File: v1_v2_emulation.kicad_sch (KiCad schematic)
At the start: 7 parts, among them CN5 LED, IC20 7407, IC65 D65101GD110

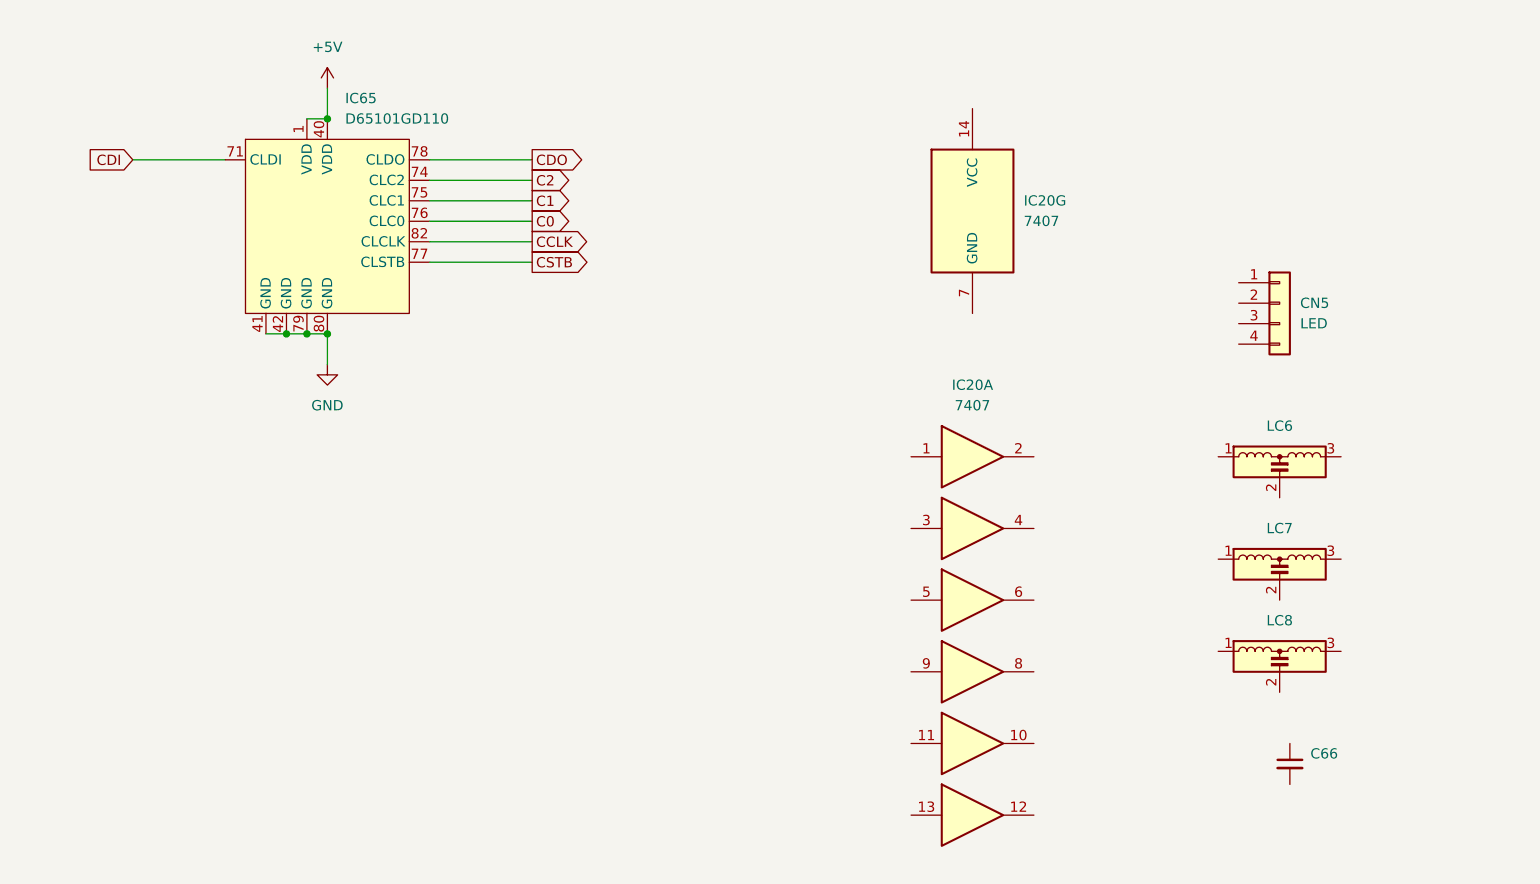
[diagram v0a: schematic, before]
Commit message: add CN2 FDD connector
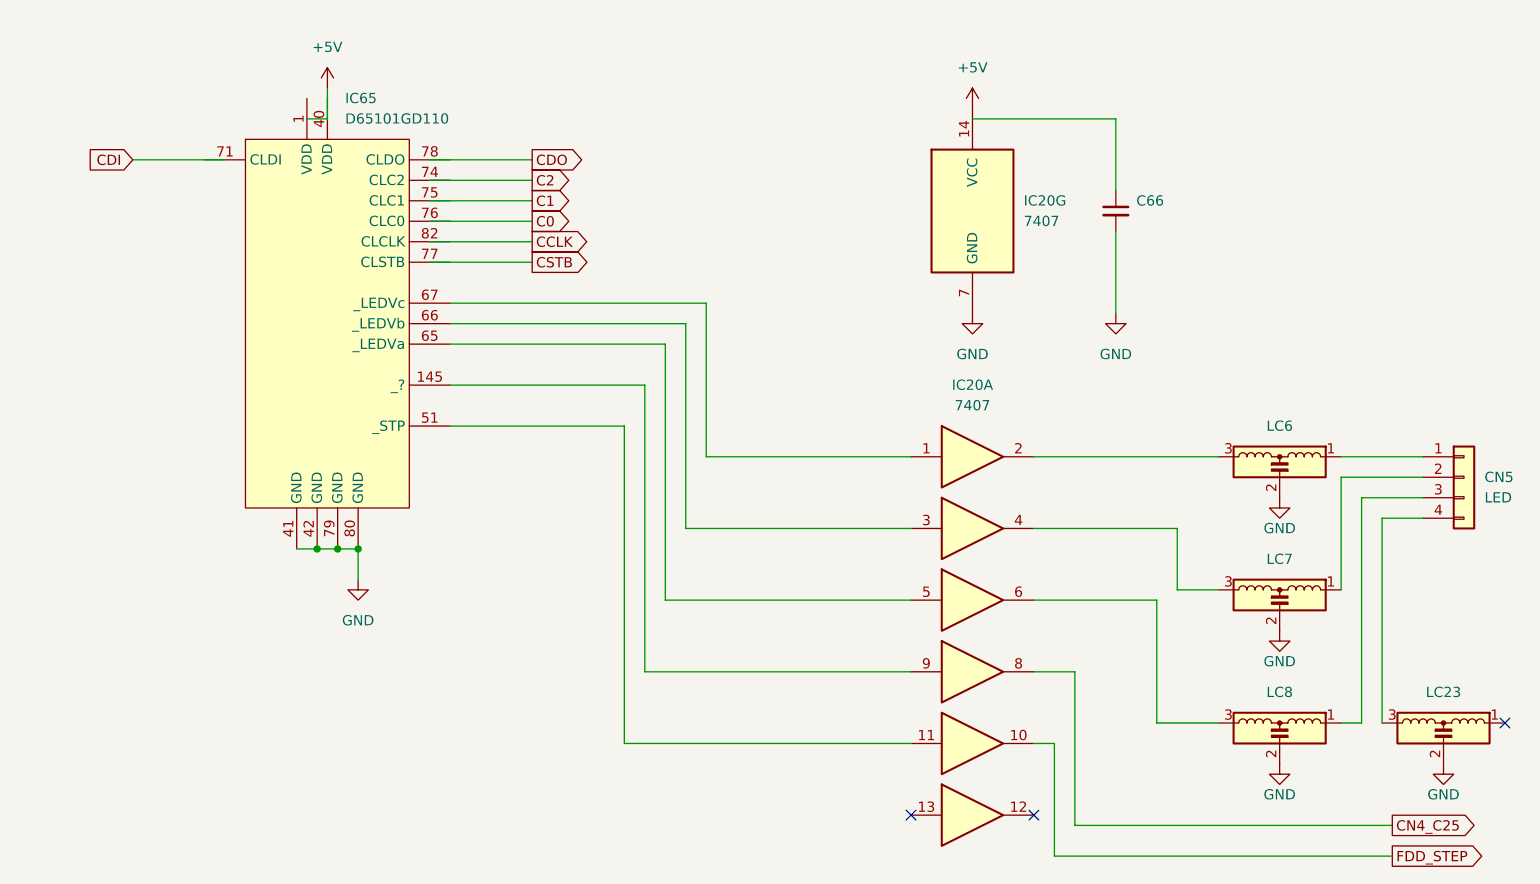
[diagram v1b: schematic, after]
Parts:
- added LC23: Filter_EMI_LCL, 88va_Library:Filter, symbol Device:Filter_EMI_LCL
- C66: footprint (none) -> Capacitor_SMD:C_1206_3216Metric
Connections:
- net +5V: now also IC20.14 (VCC); no longer IC65.1 (VDD), IC65.40 (VDD)
- net C0: no longer IC65.76 (CLC0)
- net C1: no longer IC65.75 (CLC1)
- net C2: no longer IC65.74 (CLC2)
- net CCLK: no longer IC65.82 (CLCLK)
- net CDI: no longer IC65.71 (CLDI)
- net CDO: no longer IC65.78 (CLDO)
- net CSTB: no longer IC65.77 (CLSTB)
- net GND: now also C66.2, IC20.7 (GND), LC6.2, LC7.2, LC8.2, LC23.2
- net FDD_STEP: now reaches IC20.10
- net at IC20.11: now also IC65.51 (_STP)
- net CN4_C25: now reaches IC20.8
- net at IC20.9: now also IC65.145 (_?)
- net at IC20.5: now also IC65.65 (_LEDVa)
- net at IC20.6: now also LC8.3
- net at IC20.3: now also IC65.66 (_LEDVb)
- net at IC20.4: now also LC7.3
- net at LC7.1: now also CN5.2 (Pin_2)
- net at LC6.1: now also CN5.1 (Pin_1)
- net at LC6.3: now also IC20.2
- net at IC20.1: now also IC65.67 (_LEDVc)
- net at LC8.1: now also CN5.3 (Pin_3)
- net at CN5.4 (Pin_4): now also LC23.3
- no-connect marks 0 -> 3
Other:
- moved on the sheet: C66, CN5, LC7, LC8

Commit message: add CN4 TEXT BUS
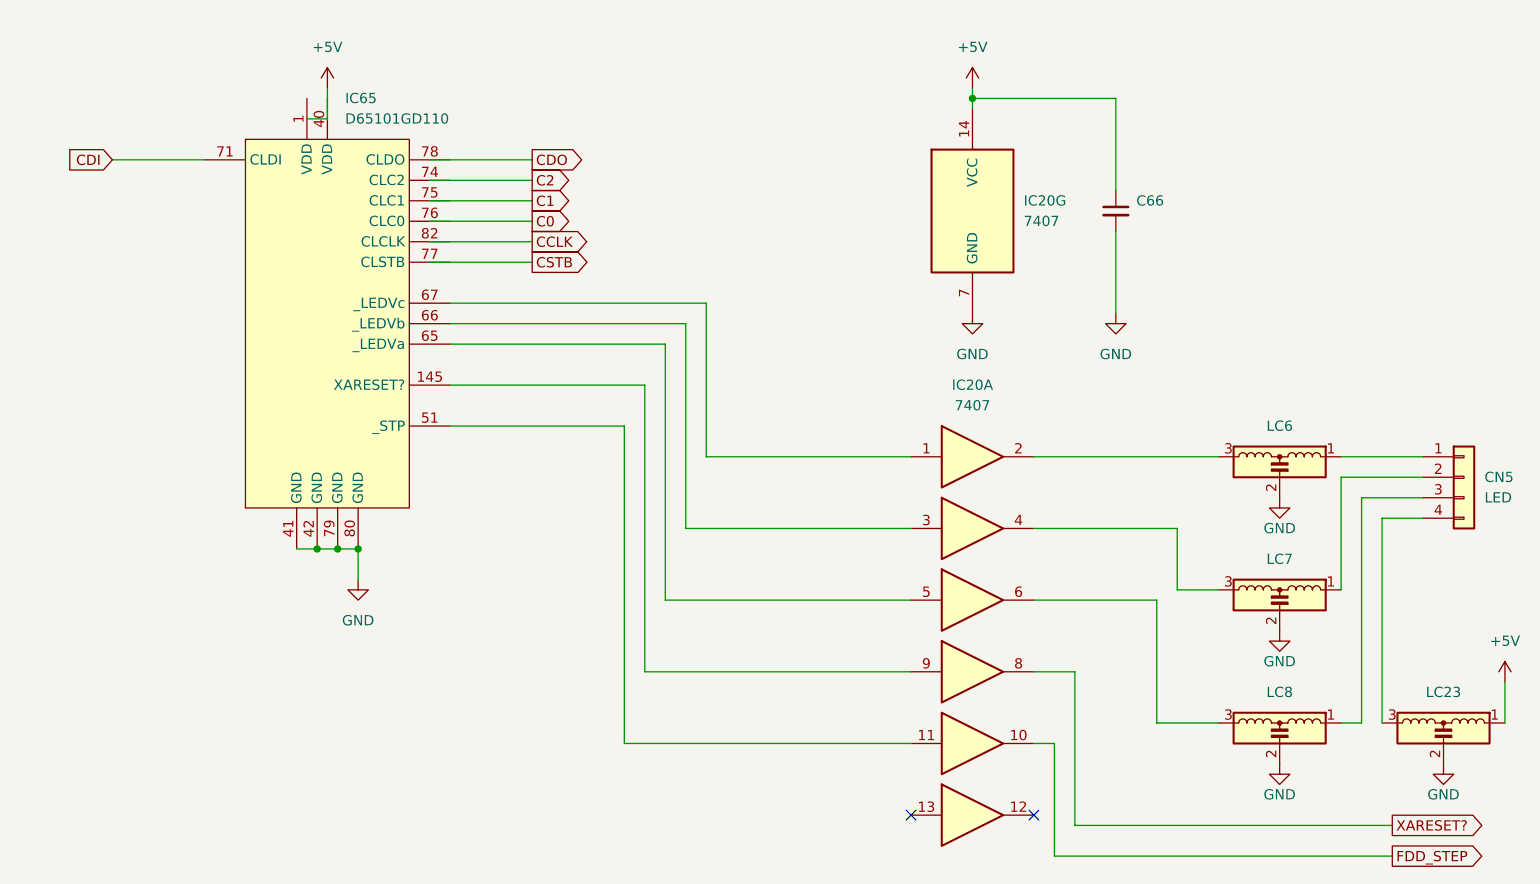
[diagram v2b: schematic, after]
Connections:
- net +5V: now also C66.1, LC23.1
- net CDI: now also IC65.71 (CLDI)
- net CN4_C25 renamed XARESET?
- no-connect marks 3 -> 2
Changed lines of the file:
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@@
   (junction (at 135.89 125.73) (diameter 0) (color 0 0 0 0)
+  )
+  (junction (at 217.17 69.85) (diameter 0) (color 0 0 0 0)
   )
   (junction (at 140.97 125.73) (diameter 0) (color 0 0 0 0)
@@
   (no_connect (at 224.79 158.75))
   (no_connect (at 209.55 158.75))
-  (no_connect (at 283.21 147.32))
-  (wire (pts (xy 234.95 72.39) (xy 234.95 81.28))
+  (wire (pts (xy 234.95 69.85) (xy 234.95 81.28))
     (stroke (width 0) (type default))
   )
@@
     (stroke (width 0) (type default))
   )
-  (wire (pts (xy 217.17 72.39) (xy 234.95 72.39))
+  (wire (pts (xy 217.17 69.85) (xy 234.95 69.85))
+    (stroke (width 0) (type default))
+  )
+  (wire (pts (xy 217.17 69.85) (xy 217.17 71.12))
     (stroke (width 0) (type default))
   )
@@
     (stroke (width 0) (type default))
   )
+  (wire (pts (xy 217.17 68.58) (xy 217.17 69.85))
+    (stroke (width 0) (type default))
+  )
   (wire (pts (xy 224.79 132.08) (xy 240.03 132.08))
     (stroke (width 0) (type default))
@@
     (stroke (width 0) (type default))
   )
-  (wire (pts (xy 113.03 77.47) (xy 124.46 77.47))
+  (wire (pts (xy 110.49 77.47) (xy 121.92 77.47))
     (stroke (width 0) (type default))
   )
@@
     (stroke (width 0) (type default))
   )
+  (wire (pts (xy 283.21 142.24) (xy 283.21 147.32))
+    (stroke (width 0) (type default))
+  )
   (wire (pts (xy 179.07 132.08) (xy 209.55 132.08))
     (stroke (width 0) (type default))
@@
     (stroke (width 0) (type default))
   )
-  (global_label "CN4_C25" (shape output) (at 269.24 160.02 0) (fields_autoplaced)
+  (global_label "XARESET?" (shape output) (at 269.24 160.02 0) (fields_autoplaced)
     (effects (font (size 1.27 1.27)) (justify left))
-    (property "Intersheetrefs" "${INTERSHEET_REFS}" (at 280.6918 160.02 0)
+    (property "Intersheetrefs" "${INTERSHEET_REFS}" (at 281.357 160.02 0)
       (effects (font (size 1.27 1.27)) (justify left) hide)
     )
@@
     )
   )
-  (global_label "CDI" (shape input) (at 113.03 77.47 180) (fields_autoplaced)
+  (global_label "CDI" (shape input) (at 110.49 77.47 180) (fields_autoplaced)
     (effects (font (size 1.27 1.27)) (justify right))
-    (property "Intersheetrefs" "${INTERSHEET_REFS}" (at 106.9 77.47 0)
+    (property "Intersheetrefs" "${INTERSHEET_REFS}" (at 104.36 77.47 0)
       (effects (font (size 1.27 1.27)) (justify right) hide)
     )
@@
     )
   )
+  (symbol (lib_id "power:+5V") (at 283.21 142.24 0) (unit 1)
+    (in_bom yes) (on_board yes) (dnp no) (fields_autoplaced)
+    (property "Reference" "#PWR024" (at 283.21 146.05 0)
+      (effects (font (size 1.27 1.27)) hide)
+    )
+    (property "Value" "+5V" (at 283.21 137.16 0)
+      (effects (font (size 1.27 1.27)))
+    )
+    (property "Footprint" "" (at 283.21 142.24 0)
+      (effects (font (size 1.27 1.27)) hide)
+    )
+    (property "Datasheet" "" (at 283.21 142.24 0)
+      (effects (font (size 1.27 1.27)) hide)
+    )
+    (pin "1")
+    (instances
+      (project "PWD665"
+        (path "/8cd193ae-a369-4130-9ba4-f2075fa60e2b/4936267e-2afc-4e41-be53-b97a571a33d1"
+          (reference "#PWR024") (unit 1)
+        )
+      )
+    )
+  )
   (symbol (lib_id "power:GND") (at 275.59 152.4 0) (unit 1)
     (in_bom yes) (on_board yes) (dnp no)
@@
     )
   )
-  (symbol (lib_id "power:+5V") (at 217.17 71.12 0) (unit 1)
-    (in_bom yes) (on_board yes) (dnp no) (fields_autoplaced)
-    (property "Reference" "#PWR018" (at 217.17 74.93 0)
-      (effects (font (size 1.27 1.27)) hide)
-    )
-    (property "Value" "+5V" (at 217.17 66.04 0)
-      (effects (font (size 1.27 1.27)))
-    )
-    (property "Footprint" "" (at 217.17 71.12 0)
-      (effects (font (size 1.27 1.27)) hide)
-    )
-    (property "Datasheet" "" (at 217.17 71.12 0)
-      (effects (font (size 1.27 1.27)) hide)
-    )
+  (symbol (lib_id "power:+5V") (at 217.17 68.58 0) (unit 1)
+    (in_bom yes) (on_board yes) (dnp no) (fields_autoplaced)
+    (property "Reference" "#PWR018" (at 217.17 72.39 0)
+      (effects (font (size 1.27 1.27)) hide)
+    )
+    (property "Value" "+5V" (at 217.17 63.5 0)
+      (effects (font (size 1.27 1.27)))
+    )
+    (property "Footprint" "" (at 217.17 68.58 0)
+      (effects (font (size 1.27 1.27)) hide)
+    )
+    (property "Datasheet" "" (at 217.17 68.58 0)
+      (effects (font (size 1.27 1.27)) hide)
+    )

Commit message: fix IC65
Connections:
- net +5V: now also IC65.1 (VDD), IC65.40 (VDD)
- net C0: now also IC65.76 (CLC0)
- net C1: now also IC65.75 (CLC1)
- net C2: now also IC65.74 (CLC2)
- net CCLK: now also IC65.82 (CLCLK)
- net CDO: now also IC65.78 (CLDO)
- net CSTB: now also IC65.77 (CLSTB)
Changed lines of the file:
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@@
   (junction (at 217.17 69.85) (diameter 0) (color 0 0 0 0)
+  )
+  (junction (at 137.16 69.85) (diameter 0) (color 0 0 0 0)
   )
   (junction (at 140.97 125.73) (diameter 0) (color 0 0 0 0)
@@
     (stroke (width 0) (type default))
   )
-  (wire (pts (xy 149.86 77.47) (xy 162.56 77.47))
+  (wire (pts (xy 152.4 77.47) (xy 162.56 77.47))
     (stroke (width 0) (type default))
   )
@@
     (stroke (width 0) (type default))
   )
-  (wire (pts (xy 137.16 68.58) (xy 137.16 72.39))
-    (stroke (width 0) (type default))
-  )
   (wire (pts (xy 217.17 69.85) (xy 234.95 69.85))
     (stroke (width 0) (type default))
@@
     (stroke (width 0) (type default))
   )
-  (wire (pts (xy 149.86 87.63) (xy 162.56 87.63))
+  (wire (pts (xy 152.4 87.63) (xy 162.56 87.63))
     (stroke (width 0) (type default))
   )
@@
     (stroke (width 0) (type default))
   )
-  (wire (pts (xy 134.62 72.39) (xy 137.16 72.39))
+  (wire (pts (xy 134.62 69.85) (xy 137.16 69.85))
     (stroke (width 0) (type default))
   )
@@
     (stroke (width 0) (type default))
   )
+  (wire (pts (xy 137.16 66.04) (xy 137.16 69.85))
+    (stroke (width 0) (type default))
+  )
   (wire (pts (xy 133.35 125.73) (xy 135.89 125.73))
     (stroke (width 0) (type default))
@@
     (stroke (width 0) (type default))
   )
-  (wire (pts (xy 149.86 82.55) (xy 162.56 82.55))
+  (wire (pts (xy 152.4 82.55) (xy 162.56 82.55))
     (stroke (width 0) (type default))
   )
@@
     (stroke (width 0) (type default))
   )
-  (wire (pts (xy 149.86 85.09) (xy 162.56 85.09))
-    (stroke (width 0) (type default))
-  )
-  (wire (pts (xy 149.86 90.17) (xy 162.56 90.17))
+  (wire (pts (xy 152.4 85.09) (xy 162.56 85.09))
+    (stroke (width 0) (type default))
+  )
+  (wire (pts (xy 152.4 90.17) (xy 162.56 90.17))
     (stroke (width 0) (type default))
   )
@@
     (stroke (width 0) (type default))
   )
-  (wire (pts (xy 149.86 80.01) (xy 162.56 80.01))
+  (wire (pts (xy 152.4 80.01) (xy 162.56 80.01))
     (stroke (width 0) (type default))
   )
@@
     (pin "2")
     (instances
-      (project "PWD665"
+      (project "88va2-circuit"
         (path "/8cd193ae-a369-4130-9ba4-f2075fa60e2b/4936267e-2afc-4e41-be53-b97a571a33d1"
           (reference "IC20") (unit 5)
@@
     (pin "2")
     (instances
-      (project "PWD665"
+      (project "88va2-circuit"
         (path "/8cd193ae-a369-4130-9ba4-f2075fa60e2b/4936267e-2afc-4e41-be53-b97a571a33d1"
           (reference "IC20") (unit 4)
@@
     (pin "67")
     (instances
-      (project "PWD665"
+      (project "88va2-circuit"
         (path "/8cd193ae-a369-4130-9ba4-f2075fa60e2b/4936267e-2afc-4e41-be53-b97a571a33d1"
           (reference "IC65") (unit 1)
@@
     )
   )
-  (symbol (lib_id "power:+5V") (at 137.16 68.58 0) (unit 1)
-    (in_bom yes) (on_board yes) (dnp no) (fields_autoplaced)
-    (property "Reference" "#PWR015" (at 137.16 72.39 0)
-      (effects (font (size 1.27 1.27)) hide)
-    )
-    (property "Value" "+5V" (at 137.16 63.5 0)
-      (effects (font (size 1.27 1.27)))
-    )
-    (property "Footprint" "" (at 137.16 68.58 0)
-      (effects (font (size 1.27 1.27)) hide)
-    )
-    (property "Datasheet" "" (at 137.16 68.58 0)
-      (effects (font (size 1.27 1.27)) hide)
-    )
-    (pin "1")
-    (instances
-      (project "PWD665"
+  (symbol (lib_id "power:+5V") (at 137.16 66.04 0) (unit 1)
+    (in_bom yes) (on_board yes) (dnp no) (fields_autoplaced)
+    (property "Reference" "#PWR015" (at 137.16 69.85 0)
+      (effects (font (size 1.27 1.27)) hide)
+    )
+    (property "Value" "+5V" (at 137.16 60.96 0)
+      (effects (font (size 1.27 1.27)))
+    )
+    (property "Footprint" "" (at 137.16 66.04 0)
+      (effects (font (size 1.27 1.27)) hide)
+    )
+    (property "Datasheet" "" (at 137.16 66.04 0)
+      (effects (font (size 1.27 1.27)) hide)
+    )
+    (pin "1")
+    (instances
+      (project "88va2-circuit"
         (path "/8cd193ae-a369-4130-9ba4-f2075fa60e2b/4936267e-2afc-4e41-be53-b97a571a33d1"
           (reference "#PWR015") (unit 1)
@@
     (pin "2")
     (instances
-      (project "PWD665"
+      (project "88va2-circuit"
         (path "/8cd193ae-a369-4130-9ba4-f2075fa60e2b/4936267e-2afc-4e41-be53-b97a571a33d1"
           (reference "IC20") (unit 3)
@@
     (pin "1")
     (instances
-      (project "PWD665"
+      (project "88va2-circuit"
         (path "/8cd193ae-a369-4130-9ba4-f2075fa60e2b/4936267e-2afc-4e41-be53-b97a571a33d1"
           (reference "C66") (unit 1)
@@
     (pin "2")
     (instances
-      (project "PWD665"
+      (project "88va2-circuit"
         (path "/8cd193ae-a369-4130-9ba4-f2075fa60e2b/4936267e-2afc-4e41-be53-b97a571a33d1"
           (reference "IC20") (unit 2)
@@
     (pin "2")
     (instances
-      (project "PWD665"
+      (project "88va2-circuit"
         (path "/8cd193ae-a369-4130-9ba4-f2075fa60e2b/4936267e-2afc-4e41-be53-b97a571a33d1"
           (reference "IC20") (unit 7)
@@
     (pin "3")
     (instances
-      (project "PWD665"
+      (project "88va2-circuit"
         (path "/8cd193ae-a369-4130-9ba4-f2075fa60e2b/4936267e-2afc-4e41-be53-b97a571a33d1"
           (reference "LC7") (unit 1)
@@
     (pin "1")
     (instances
-      (project "PWD665"
+      (project "88va2-circuit"
         (path "/8cd193ae-a369-4130-9ba4-f2075fa60e2b/4936267e-2afc-4e41-be53-b97a571a33d1"
           (reference "#PWR021") (unit 1)
@@
     (pin "2")
     (instances
-      (project "PWD665"
+      (project "88va2-circuit"
         (path "/8cd193ae-a369-4130-9ba4-f2075fa60e2b/4936267e-2afc-4e41-be53-b97a571a33d1"
           (reference "IC20") (unit 6)
@@
     (pin "1")
     (instances
-      (project "PWD665"
+      (project "88va2-circuit"
         (path "/8cd193ae-a369-4130-9ba4-f2075fa60e2b/4936267e-2afc-4e41-be53-b97a571a33d1"
           (reference "#PWR020") (unit 1)
@@
     (pin "3")
     (instances
-      (project "PWD665"
+      (project "88va2-circuit"
         (path "/8cd193ae-a369-4130-9ba4-f2075fa60e2b/4936267e-2afc-4e41-be53-b97a571a33d1"
           (reference "LC6") (unit 1)
@@
     (pin "1")
     (instances
-      (project "PWD665"
+      (project "88va2-circuit"
         (path "/8cd193ae-a369-4130-9ba4-f2075fa60e2b/4936267e-2afc-4e41-be53-b97a571a33d1"
           (reference "#PWR016") (unit 1)
@@
     (pin "2")
     (instances
-      (project "PWD665"
+      (project "88va2-circuit"
         (path "/8cd193ae-a369-4130-9ba4-f2075fa60e2b/4936267e-2afc-4e41-be53-b97a571a33d1"
           (reference "IC20") (unit 1)
@@
     (pin "1")
     (instances
-      (project "PWD665"
+      (project "88va2-circuit"
         (path "/8cd193ae-a369-4130-9ba4-f2075fa60e2b/4936267e-2afc-4e41-be53-b97a571a33d1"
           (reference "#PWR022") (unit 1)
@@
     (pin "1")
     (instances
-      (project "PWD665"
+      (project "88va2-circuit"
         (path "/8cd193ae-a369-4130-9ba4-f2075fa60e2b/4936267e-2afc-4e41-be53-b97a571a33d1"
           (reference "#PWR024") (unit 1)
@@
     (pin "1")
     (instances
-      (project "PWD665"
+      (project "88va2-circuit"
         (path "/8cd193ae-a369-4130-9ba4-f2075fa60e2b/4936267e-2afc-4e41-be53-b97a571a33d1"
           (reference "#PWR019") (unit 1)
@@
     (pin "1")
     (instances
-      (project "PWD665"
+      (project "88va2-circuit"
         (path "/8cd193ae-a369-4130-9ba4-f2075fa60e2b/4936267e-2afc-4e41-be53-b97a571a33d1"
           (reference "#PWR014") (unit 1)
@@
     (pin "3")
     (instances
-      (project "PWD665"
+      (project "88va2-circuit"
         (path "/8cd193ae-a369-4130-9ba4-f2075fa60e2b/4936267e-2afc-4e41-be53-b97a571a33d1"
           (reference "LC8") (unit 1)
@@
     (pin "3")
     (instances
-      (project "PWD665"
+      (project "88va2-circuit"
         (path "/8cd193ae-a369-4130-9ba4-f2075fa60e2b/4936267e-2afc-4e41-be53-b97a571a33d1"
           (reference "LC23") (unit 1)
@@
     (pin "2")
     (instances
-      (project "PWD665"
+      (project "88va2-circuit"
         (path "/8cd193ae-a369-4130-9ba4-f2075fa60e2b/4936267e-2afc-4e41-be53-b97a571a33d1"
           (reference "CN5") (unit 1)
@@
     (pin "1")
     (instances
-      (project "PWD665"
+      (project "88va2-circuit"
         (path "/8cd193ae-a369-4130-9ba4-f2075fa60e2b/4936267e-2afc-4e41-be53-b97a571a33d1"
           (reference "#PWR017") (unit 1)
@@
     (pin "1")
     (instances
-      (project "PWD665"
+      (project "88va2-circuit"
         (path "/8cd193ae-a369-4130-9ba4-f2075fa60e2b/4936267e-2afc-4e41-be53-b97a571a33d1"
           (reference "#PWR018") (unit 1)
